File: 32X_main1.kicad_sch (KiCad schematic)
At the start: 27 parts, among them IC504 315-5818, IC505 315-5805, IC509 74AC04

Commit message: Enlarge some footprints, fix unwanted A/D ground connections.
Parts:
- IC509: footprint Package_SO:SO-14_3.9x8.65mm_P1.27mm -> Package_SO:SO-14_5.3x10.2mm_P1.27mm
- L501: footprint Inductor_SMD:L_0805_2012Metric -> Inductor_SMD:L_1206_3216Metric
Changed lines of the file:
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@@
       (effects (font (size 1.27 1.27)))
     )
-    (property "Footprint" "Package_SO:SO-14_3.9x8.65mm_P1.27mm" (at 135.89 237.49 0)
+    (property "Footprint" "Package_SO:SO-14_5.3x10.2mm_P1.27mm" (at 135.89 237.49 0)
       (effects (font (size 1.27 1.27)) hide)
     )
@@
       (effects (font (size 1.27 1.27)) (justify left))
     )
-    (property "Footprint" "Package_SO:SO-14_3.9x8.65mm_P1.27mm" (at 257.81 251.46 0)
+    (property "Footprint" "Package_SO:SO-14_5.3x10.2mm_P1.27mm" (at 257.81 251.46 0)
       (effects (font (size 1.27 1.27)) hide)
     )
@@
       (effects (font (size 1.27 1.27)))
     )
-    (property "Footprint" "Package_SO:SO-14_3.9x8.65mm_P1.27mm" (at 156.845 237.49 0)
+    (property "Footprint" "Package_SO:SO-14_5.3x10.2mm_P1.27mm" (at 156.845 237.49 0)
       (effects (font (size 1.27 1.27)) hide)
     )
@@
       (effects (font (size 1.27 1.27)))
     )
-    (property "Footprint" "Package_SO:SO-14_3.9x8.65mm_P1.27mm" (at 118.11 156.845 0)
+    (property "Footprint" "Package_SO:SO-14_5.3x10.2mm_P1.27mm" (at 118.11 156.845 0)
       (effects (font (size 1.27 1.27)) hide)
     )
@@
       (effects (font (size 1.27 1.27)) (justify left))
     )
-    (property "Footprint" "Inductor_SMD:L_0805_2012Metric" (at 203.835 170.815 0)
+    (property "Footprint" "Inductor_SMD:L_1206_3216Metric" (at 203.835 170.815 0)
       (effects (font (size 1.27 1.27)) hide)
     )
@@
       (effects (font (size 1.27 1.27)))
     )
-    (property "Footprint" "Package_SO:SO-14_3.9x8.65mm_P1.27mm" (at 249.555 203.2 0)
-      (effects (font (size 1.27 1.27)) hide)
-    )
+    (property "Footprint" "Package_SO:SO-14_5.3x10.2mm_P1.27mm" (at 249.555 203.2 0)
+      (effects (font (size 1.27 1.27)) hide)
+    )

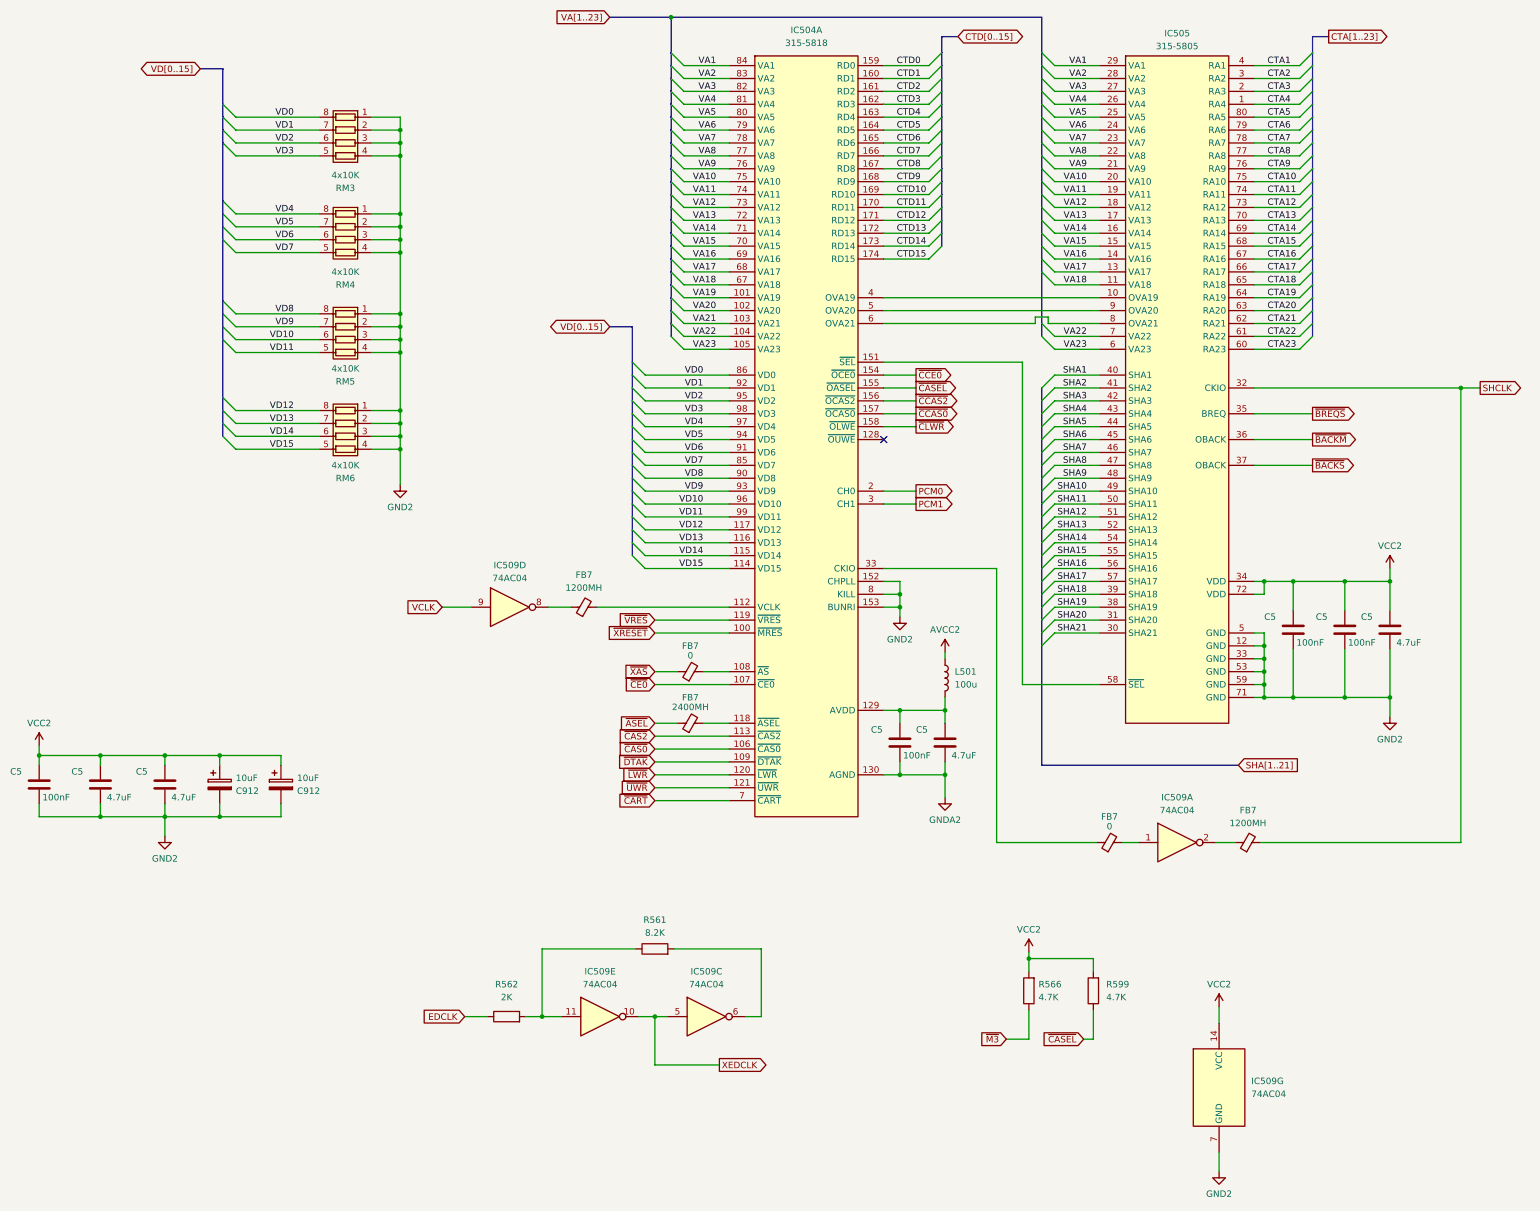
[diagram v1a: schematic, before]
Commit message: Apply fixes for issues found on prototype board.
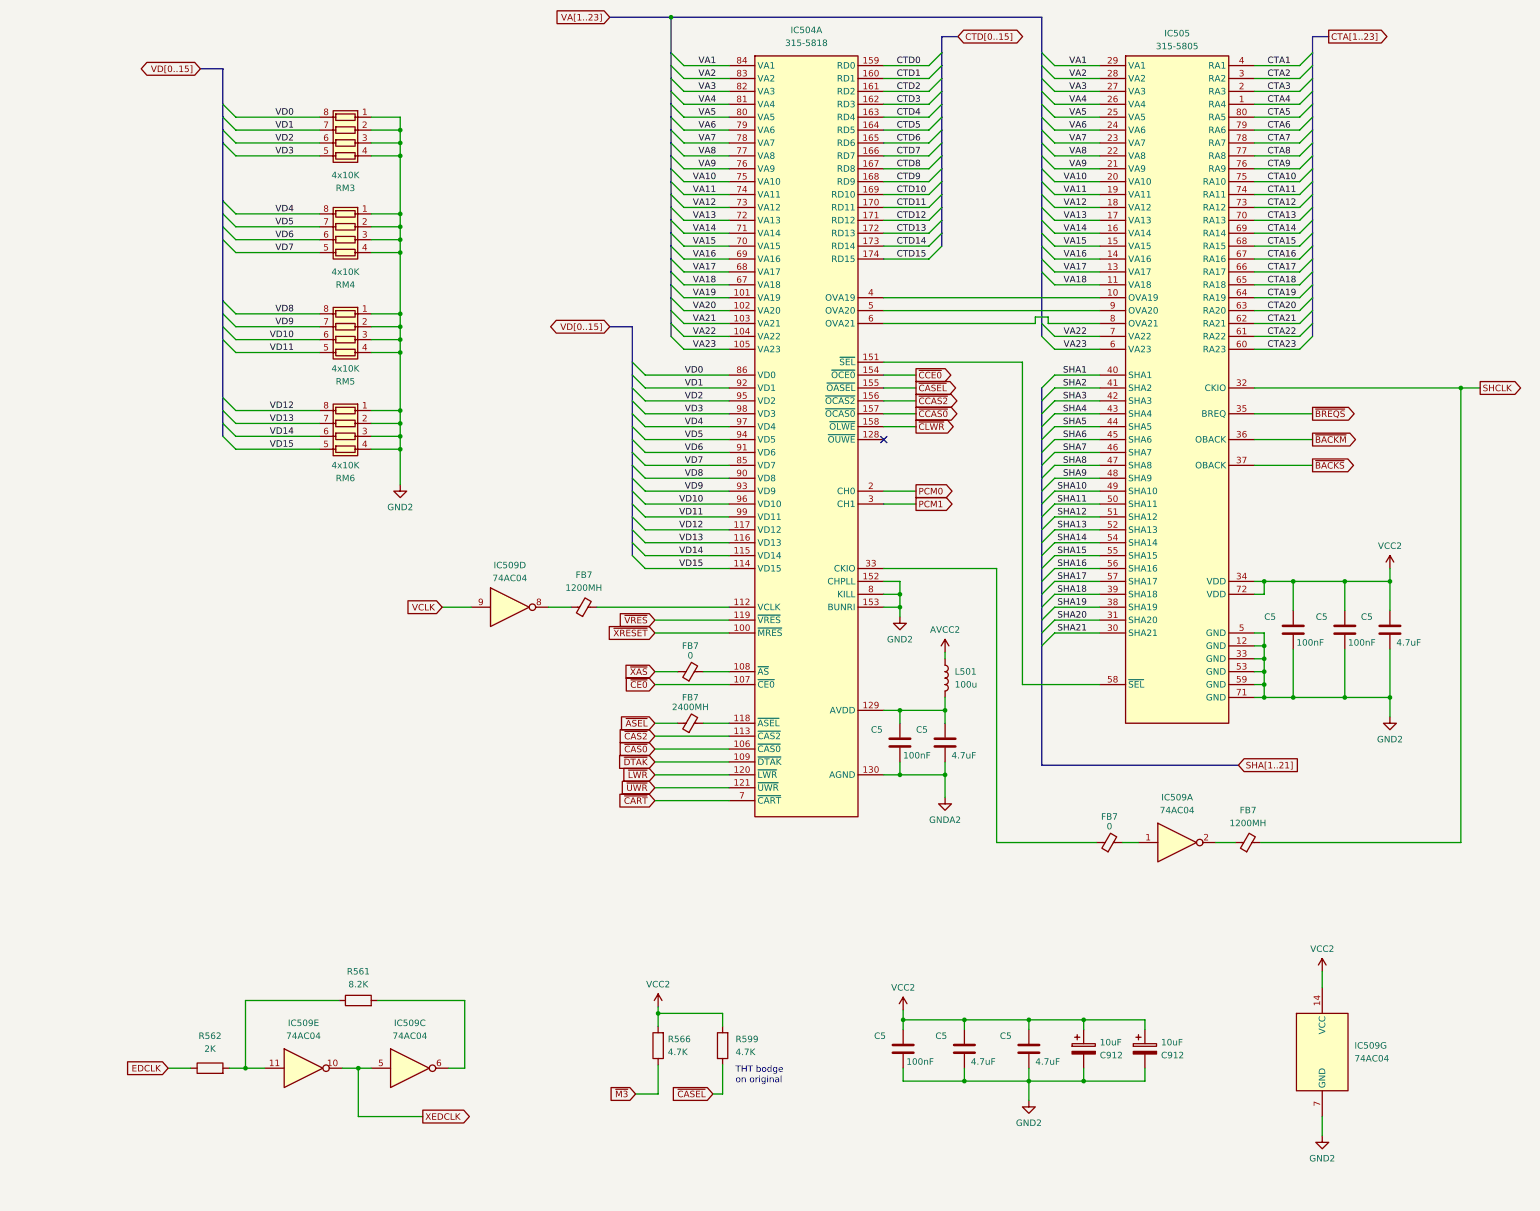
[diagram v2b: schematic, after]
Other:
- note added: "THT bodge on original"
- moved on the sheet: C5, C912, IC509C, IC509E, IC509G, R561, R562, R566, R599

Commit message: Check through 32X VA0/VA1 differences/bodges.
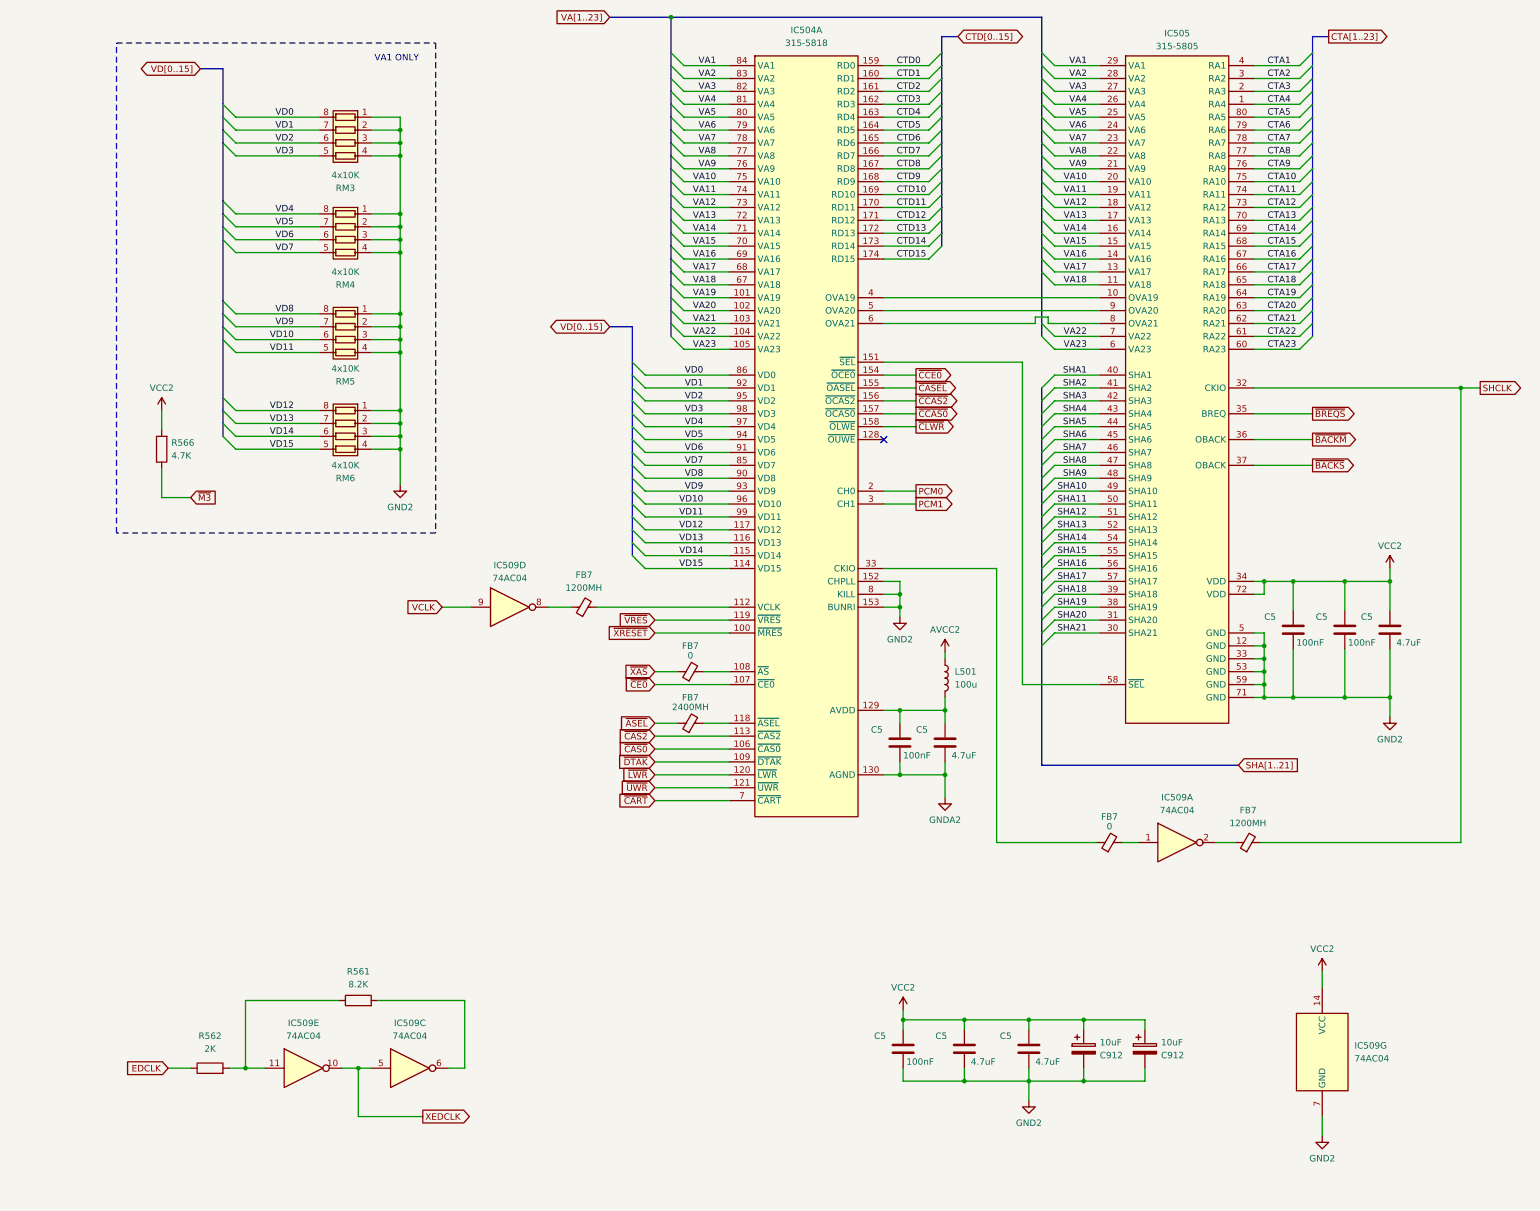
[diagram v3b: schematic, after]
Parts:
- removed R599: 4.7K, Resistor_SMD:R_0805_2012Metric, symbol Device:R
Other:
- note added: "VA1 ONLY"
- note removed: "THT bodge on original"
- moved on the sheet: R566
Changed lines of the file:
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@@
   (junction (at 194.945 177.165) (diameter 0) (color 0 0 0 0)
   )
-  (junction (at 147.32 236.855) (diameter 0) (color 0 0 0 0)
-  )
   (junction (at 194.945 154.305) (diameter 0) (color 0 0 0 0)
   )
@@
     (stroke (width 0) (type default))
   )
-  (wire (pts (xy 147.32 247.015) (xy 147.32 252.73))
+  (wire (pts (xy 49.53 129.54) (xy 49.53 135.255))
     (stroke (width 0) (type default))
   )
@@
     (stroke (width 0) (type default))
   )
-  (wire (pts (xy 158.115 252.73) (xy 160.02 252.73))
-    (stroke (width 0) (type default))
-  )
   (bus (pts (xy 222.885 88.265) (xy 222.885 85.725))
     (stroke (width 0) (type default))
@@
     (stroke (width 0) (type default))
   )
-  (wire (pts (xy 147.32 235.585) (xy 147.32 236.855))
+  (wire (pts (xy 49.53 118.11) (xy 49.53 121.92))
     (stroke (width 0) (type default))
   )
@@
     (stroke (width 0) (type default))
   )
-  (wire (pts (xy 160.02 247.015) (xy 160.02 252.73))
-    (stroke (width 0) (type default))
-  )
   (wire (pts (xy 64.135 86.995) (xy 80.645 86.995))
     (stroke (width 0) (type default))
@@
     (stroke (width 0) (type default))
   )
-  (wire (pts (xy 160.02 236.855) (xy 160.02 239.395))
-    (stroke (width 0) (type default))
-  )
   (wire (pts (xy 234.315 55.245) (xy 225.425 55.245))
     (stroke (width 0) (type default))
@@
     (stroke (width 0) (type default))
   )
-  (wire (pts (xy 147.32 236.855) (xy 160.02 236.855))
-    (stroke (width 0) (type default))
-  )
   (wire (pts (xy 191.77 73.025) (xy 200.66 73.025))
     (stroke (width 0) (type default))
@@
     (stroke (width 0) (type default))
   )
-  (wire (pts (xy 142.875 252.73) (xy 147.32 252.73))
+  (wire (pts (xy 55.245 135.255) (xy 49.53 135.255))
     (stroke (width 0) (type default))
   )
@@
     (stroke (width 0) (type default))
   )
-  (wire (pts (xy 147.32 236.855) (xy 147.32 239.395))
-    (stroke (width 0) (type default))
-  )
   (wire (pts (xy 234.315 75.565) (xy 225.425 75.565))
     (stroke (width 0) (type default))
@@
     (stroke (width 0) (type default))
   )
-  (text "THT bodge\non original" (at 162.56 250.825 0)
+  (rectangle (start 40.64 45.72) (end 103.505 142.24)
+    (stroke (width 0) (type dash))
+    (fill (type none))
+  )
+  (text "VA1 ONLY" (at 91.44 49.53 0)
     (effects (font (size 1.27 1.27)) (justify left bottom))
   )
@@
     )
   )
-  (global_label "~{CASEL}" (shape input) (at 158.115 252.73 180) (fields_autoplaced)
-    (effects (font (size 1.27 1.27)) (justify right))
-    (property "Intersheetrefs" "${INTERSHEET_REFS}" (at 149.3846 252.73 0)
-      (effects (font (size 1.27 1.27)) (justify right) hide)
-    )
-  )
   (global_label "VCLK" (shape input) (at 104.775 156.845 180) (fields_autoplaced)
     (effects (font (size 1.27 1.27)) (justify right))
@@
     )
   )
-  (global_label "~{M3}" (shape input) (at 142.875 252.73 180) (fields_autoplaced)
-    (effects (font (size 1.27 1.27)) (justify right))
-    (property "Intersheetrefs" "${INTERSHEET_REFS}" (at 137.2289 252.73 0)
-      (effects (font (size 1.27 1.27)) (justify right) hide)
+  (global_label "~{M3}" (shape input) (at 55.245 135.255 0) (fields_autoplaced)
+    (effects (font (size 1.27 1.27)) (justify left))
+    (property "Intersheetrefs" "${INTERSHEET_REFS}" (at 60.8911 135.255 0)
+      (effects (font (size 1.27 1.27)) (justify left) hide)
     )
   )
@@
     )
   )
-  (symbol (lib_id "Device:R") (at 147.32 243.205 180) (unit 1)
+  (symbol (lib_id "Device:R") (at 49.53 125.73 180) (unit 1)
     (in_bom yes) (on_board yes) (dnp no) (fields_autoplaced)
-    (property "Reference" "R566" (at 149.225 241.935 0)
+    (property "Reference" "R566" (at 51.435 124.46 0)
       (effects (font (size 1.27 1.27)) (justify right))
     )
-    (property "Value" "4.7K" (at 149.225 244.475 0)
+    (property "Value" "4.7K" (at 51.435 127 0)
       (effects (font (size 1.27 1.27)) (justify right))
     )
-    (property "Footprint" "Resistor_SMD:R_0805_2012Metric" (at 149.098 243.205 90)
+    (property "Footprint" "Resistor_SMD:R_0805_2012Metric" (at 51.308 125.73 90)
       (effects (font (size 1.27 1.27)) hide)
     )
-    (property "Datasheet" "~" (at 147.32 243.205 0)
+    (property "Datasheet" "~" (at 49.53 125.73 0)
       (effects (font (size 1.27 1.27)) hide)
     )
-    (property "DigiKey" "" (at 147.32 243.205 0)
+    (property "DigiKey" "" (at 49.53 125.73 0)
       (effects (font (size 1.27 1.27)) hide)
     )
@@
     )
   )
-  (symbol (lib_id "Device:R") (at 160.02 243.205 180) (unit 1)
-    (in_bom yes) (on_board yes) (dnp no) (fields_autoplaced)
-    (property "Reference" "R599" (at 162.56 241.935 0)
-      (effects (font (size 1.27 1.27)) (justify right))
-    )
-    (property "Value" "4.7K" (at 162.56 244.475 0)
-      (effects (font (size 1.27 1.27)) (justify right))
-    )
-    (property "Footprint" "Resistor_SMD:R_0805_2012Metric" (at 161.798 243.205 90)
-      (effects (font (size 1.27 1.27)) hide)
-    )
-    (property "Datasheet" "~" (at 160.02 243.205 0)
-      (effects (font (size 1.27 1.27)) hide)
-    )
-    (property "DigiKey" "" (at 160.02 243.205 0)
-      (effects (font (size 1.27 1.27)) hide)
-    )
-    (pin "1")
-    (pin "2")
-    (instances
-      (project "Neptune"
-        (path "/bcc23b51-b742-4ae5-9dd6-d96a24058944/a9caee2e-423b-443e-a11f-5841882e2685"
-          (reference "R599") (unit 1)
-        )
-      )
-    )
-  )
   (symbol (lib_id "Device:FerriteBead_Small") (at 153.67 169.545 90) (unit 1)
     (in_bom yes) (on_board yes) (dnp no)
@@
     )
   )
-  (symbol (lib_id "32X:VCC2") (at 147.32 235.585 0) (unit 1)
+  (symbol (lib_id "32X:VCC2") (at 49.53 118.11 0) (unit 1)
     (in_bom yes) (on_board yes) (dnp no) (fields_autoplaced)
-    (property "Reference" "#PWR055" (at 147.32 239.395 0)
+    (property "Reference" "#PWR055" (at 49.53 121.92 0)
       (effects (font (size 1.27 1.27)) hide)
     )
-    (property "Value" "VCC2" (at 147.32 231.14 0)
+    (property "Value" "VCC2" (at 49.53 113.665 0)
       (effects (font (size 1.27 1.27)))
     )
-    (property "Footprint" "" (at 147.32 235.585 0)
+    (property "Footprint" "" (at 49.53 118.11 0)
       (effects (font (size 1.27 1.27)) hide)
     )
-    (property "Datasheet" "" (at 147.32 235.585 0)
+    (property "Datasheet" "" (at 49.53 118.11 0)
       (effects (font (size 1.27 1.27)) hide)
     )
